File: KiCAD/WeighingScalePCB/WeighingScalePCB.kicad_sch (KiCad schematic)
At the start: 62 parts, among them IC1 MAX6675ISA+T, IC2 APS11753KMDALX-9PL5, J1 Conn_01x04_Pin, J2 AudioJack4, J3 CONN_14_FFC/FPC, J4 Battery Conn, J5 buzzer conn, Q1 MMBT2222A, Q2 NX138AKR, Q3 NX138AKR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

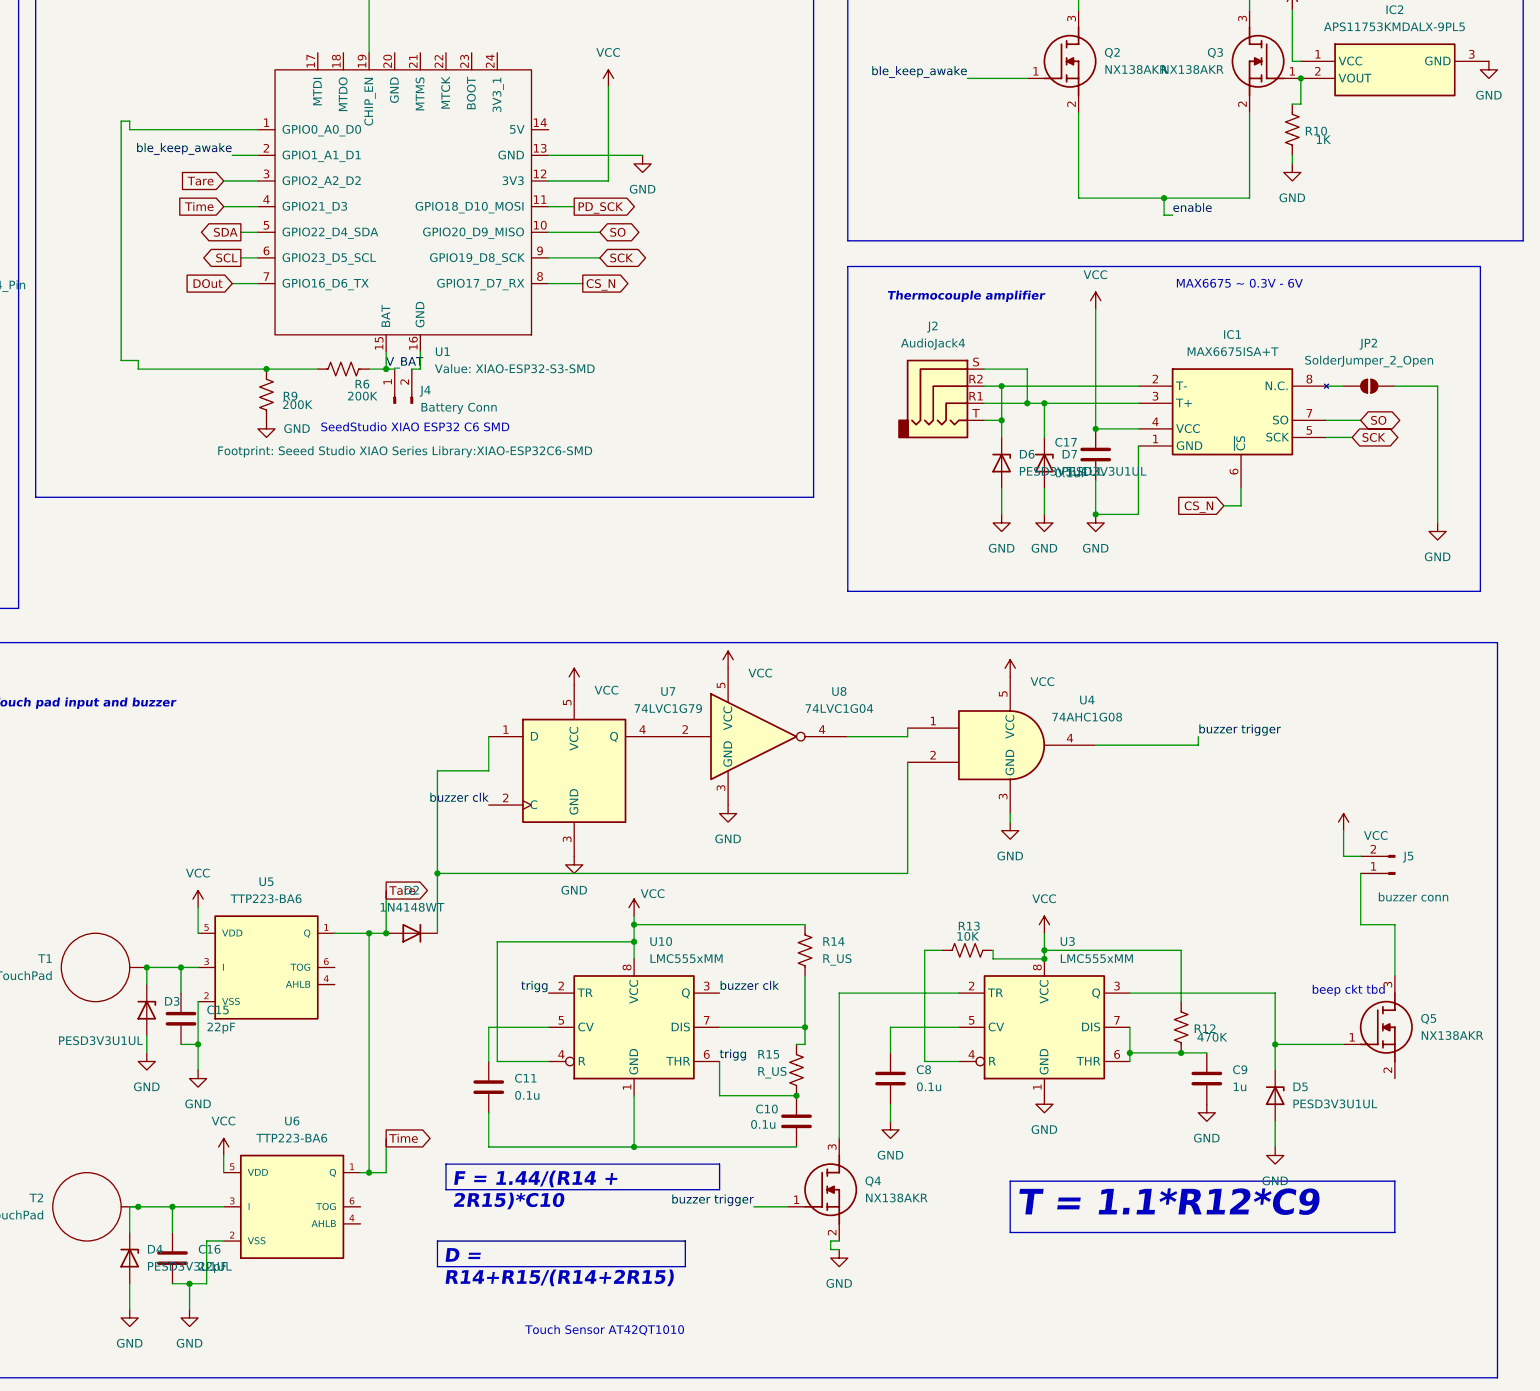
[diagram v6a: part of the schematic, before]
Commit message: 1. added TOG = 0 and AHLB = 0 for direct mode and active high setting. 2. made all digital ICs LVCMOS
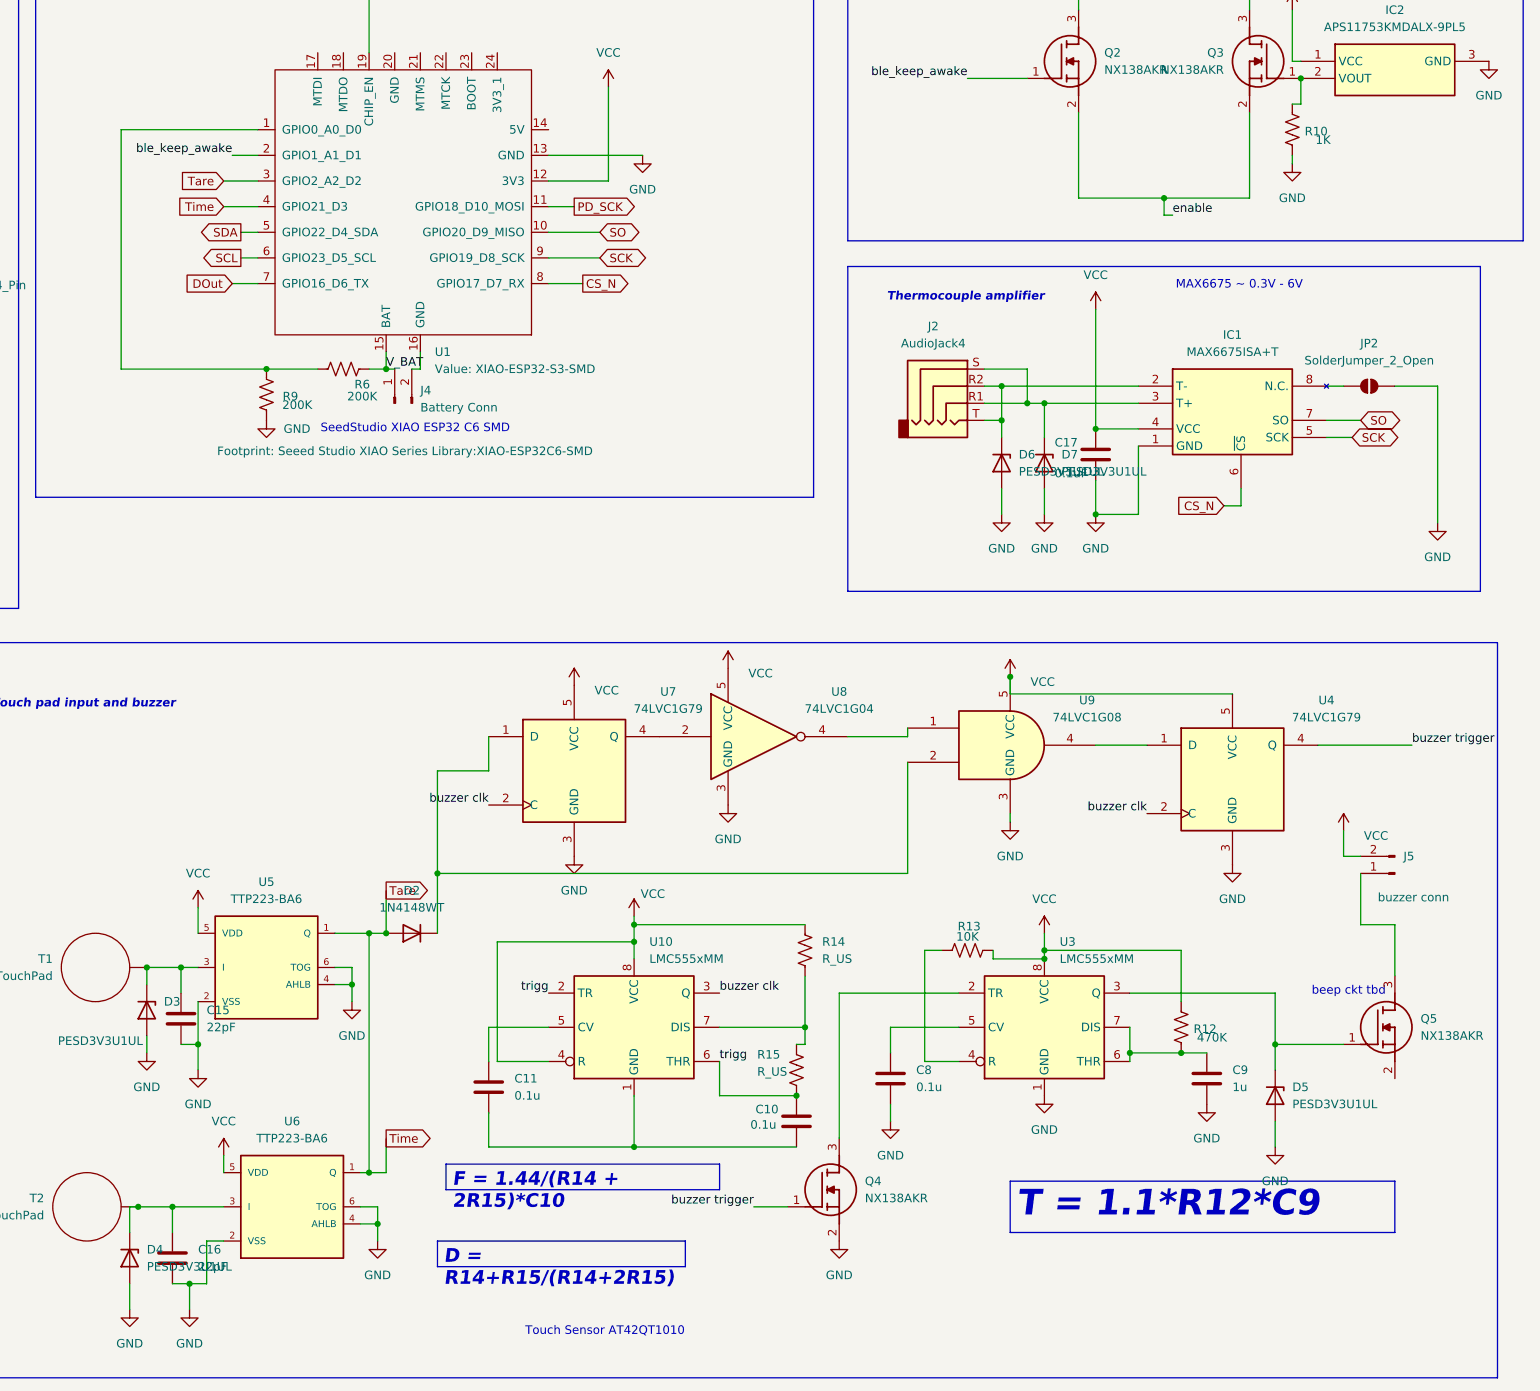
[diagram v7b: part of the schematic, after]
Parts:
- removed U4: 74AHC1G08, symbol 74xGxx:74AHC1G08
- added U4: 74LVC1G79, symbol 74xGxx:74LVC1G79
- added U9: 74LVC1G08, symbol 74xGxx:74LVC1G08
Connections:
- net GND: now also U5.4 (AHLB), U5.6 (TOG), U6.4 (AHLB), U6.6 (TOG), U4.3 (GND), U9.3 (GND)
- net VCC: now also U4.5 (VCC), U9.5 (VCC)
- net buzzer clk: now also U4.2 (C)
- net buzzer trigger: now also U4.4 (Q)
- net at U8.4: now also U9.1
- net at D2.1 (K), U7.1 (D): now also U9.2
- new net: U4.1 (D), U9.4

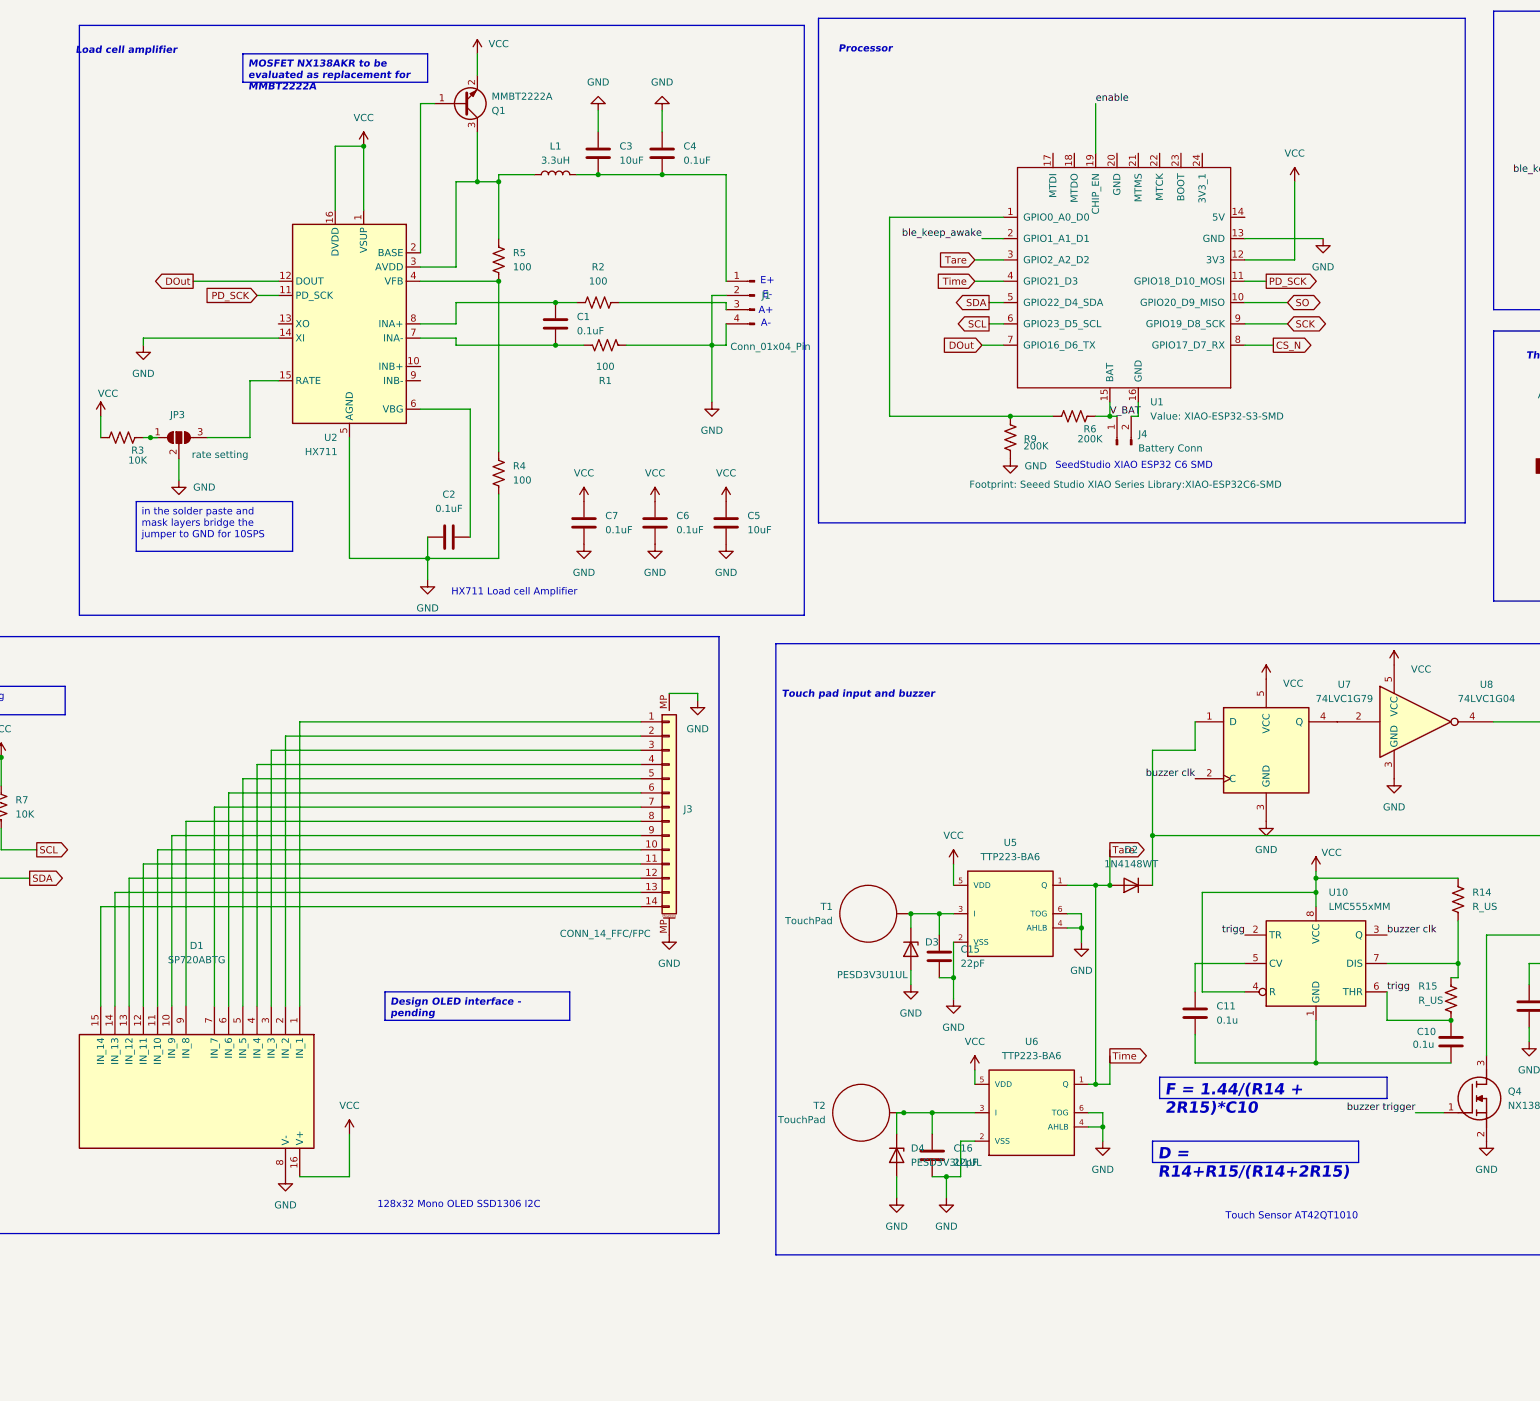
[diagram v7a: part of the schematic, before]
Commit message: made all passives 0603, added design notes, added fb between avdd and dvdd in hx711, removed transistor in hx711.
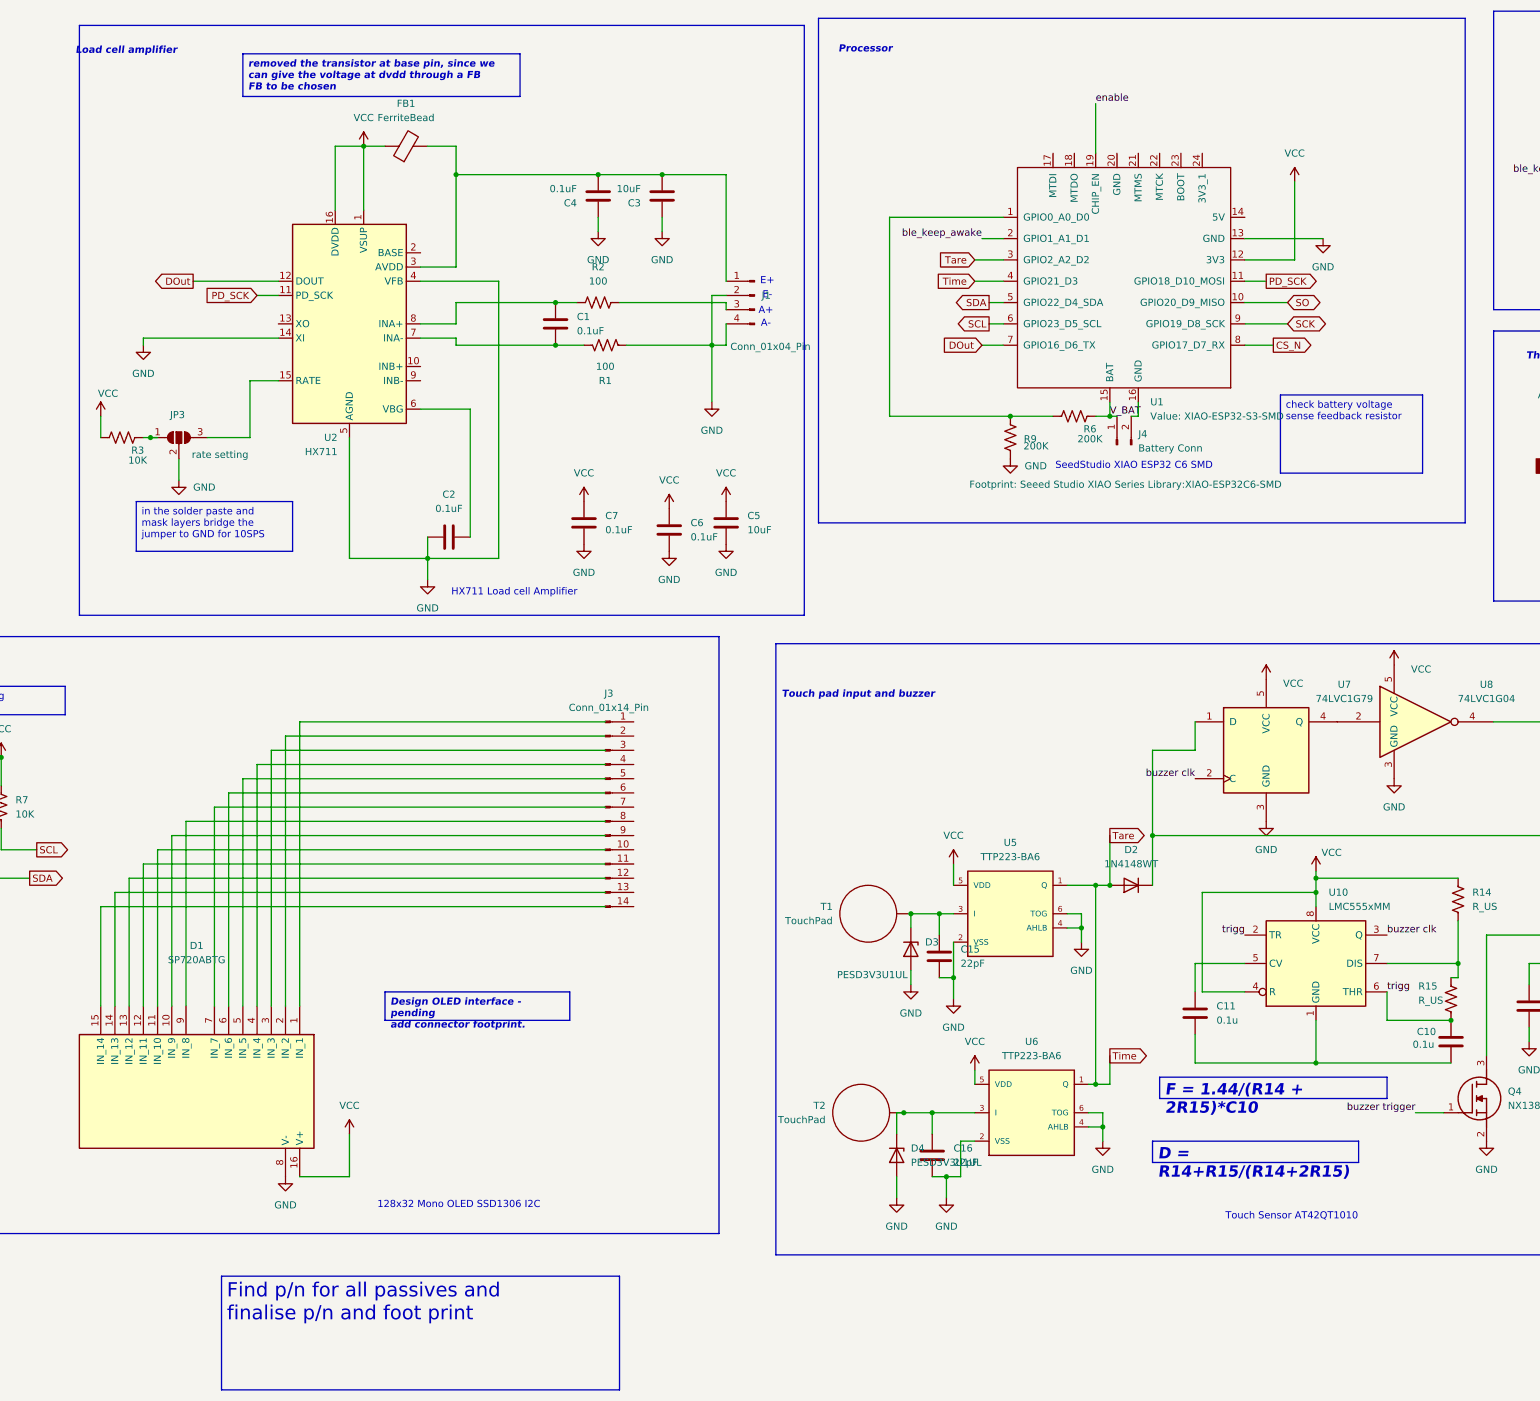
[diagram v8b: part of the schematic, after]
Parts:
- removed J3: CONN_14_FFC/FPC, symbol Connector_Generic_MountingPin:Conn_01x14_MountingPin
- removed L1: 3.3uH, Inductor_SMD:L_Coilcraft_XxL4040, symbol Device:L
- removed Q1: MMBT2222A, Package_TO_SOT_SMD:SOT-23, symbol Transistor_BJT:MMBT2222A
- removed R4, R5: 100, Resistor_SMD:R_0402_1005Metric, symbol Device:R_US
- added FB1: FerriteBead, symbol Device:FerriteBead
- added J3: Conn_01x14_Pin, symbol Connector:Conn_01x14_Pin
- C1, C10, C11, C15, C16, C17, C2, C3, C4, C5, C6, C7, C8, C9: footprint Capacitor_SMD:C_0402_1005Metric -> Capacitor_SMD:C_0603_1608Metric
- R1, R10, R11, R12, R13, R2, R3, R6, R9: footprint Resistor_SMD:R_0402_1005Metric -> Resistor_SMD:R_0603_1608Metric
- R14, R15: footprint (none) -> Resistor_SMD:R_0603_1608Metric
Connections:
- net GND: now also U2.4 (VFB)
- net VCC: now also FB1.1
- net at U2.3 (AVDD): now also C3.2, C4.2, J1.1 (Pin_1), FB1.2
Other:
- moved on the sheet: C3, C4
